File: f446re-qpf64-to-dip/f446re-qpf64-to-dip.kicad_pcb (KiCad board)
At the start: 2 copper layers, 34.5 x 83 mm, 3 parts, among them J1 Conn_01x32_Pin, J2 Conn_01x32_Pin, U1 STM32F446RETx

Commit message: change: GNDベタをやめた
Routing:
- added copper zone on F.Cu, net (none)
- removed copper zone on F.Cu, net GND
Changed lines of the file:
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@@
 		(tags "Through hole socket strip THT 1x32 2.54mm single row")
 		(property "Reference" "J2"
-			(at 0 -2.77 360)
+			(at 0 -2.77 0)
 			(layer "F.SilkS")
 			(hide yes)
@@
 		)
 		(property "Value" "Conn_01x32_Pin"
-			(at 0 81.51 360)
+			(at 0 81.51 0)
 			(layer "F.Fab")
 			(effects
@@
 	)
 	(zone
-		(net 60)
-		(net_name "GND")
+		(net 0)
+		(net_name "")
 		(layer "F.Cu")
 		(hatch edge 0.5)

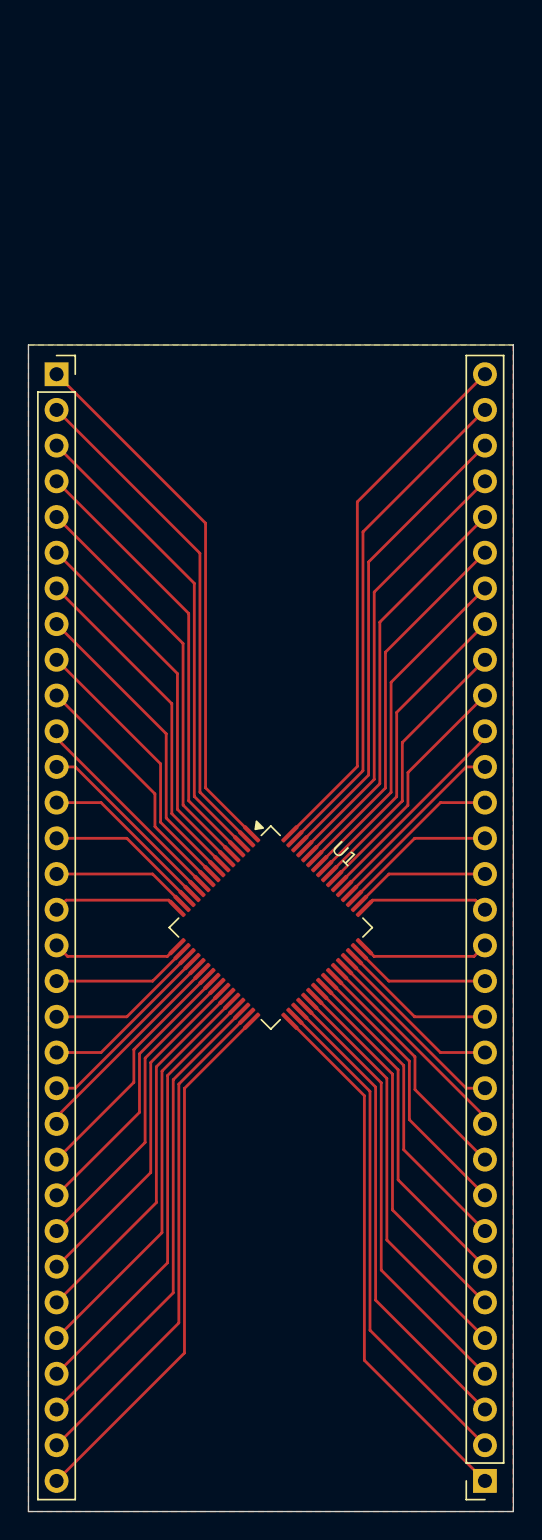
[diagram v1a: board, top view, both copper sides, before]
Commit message: change: 基盤サイズ変更
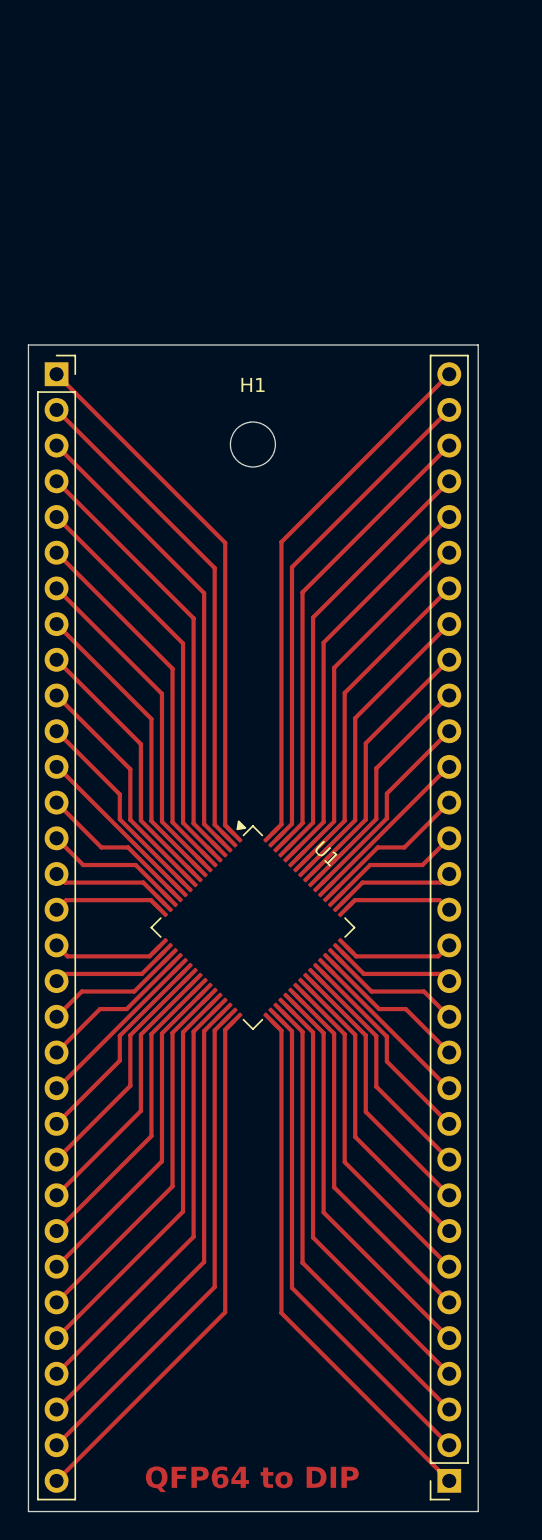
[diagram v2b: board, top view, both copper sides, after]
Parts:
- added H1: MountingHole, MountingHole:MountingHole_3.2mm_M3, F.Cu at (107.0, 88.6)
- moved J2 2.54 mm to (120.9, 162.3)
- moved U1 1.27 mm to (107.0, 123.0)
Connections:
- net GND renamed Net-(J1-Pin_18)
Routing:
- net Net-(J1-Pin_18): track 91.8 -> 88.2 mm
- net Net-(J2-Pin_21): track 13.6 -> 12.3 mm
- net Net-(J2-Pin_18): track 9.80 -> 8.53 mm
- net Net-(J2-Pin_12): track 13.6 -> 12.3 mm
- net Net-(J1-Pin_21): track 13.6 -> 12.3 mm
- net Net-(J1-Pin_12): track 13.6 -> 12.3 mm
- net Net-(J2-Pin_19): track 11.1 -> 9.79 mm
- net Net-(J2-Pin_14): track 11.1 -> 9.79 mm
- net Net-(J2-Pin_16): track 9.18 -> 7.91 mm
- net Net-(J2-Pin_13): track 12.3 -> 11.0 mm
- net Net-(J1-Pin_17): track 9.18 -> 7.91 mm
- net Net-(J1-Pin_14): track 11.1 -> 9.79 mm
- net Net-(J2-Pin_20): track 12.3 -> 11.0 mm
- net Net-(J1-Pin_13): track 12.3 -> 11.0 mm
- net Net-(J1-Pin_20): track 12.3 -> 11.0 mm
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- removed copper zone on F.Cu, net (none)
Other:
- board size 34.5 x 83 mm -> 32 x 83 mm
- board text added: "QFP64 to DIP"

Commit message: change: 配線変更
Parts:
- moved J2 21.2 mm to (117.0, 141.5)
- moved U1 20.9 mm to (105.6, 102.1)
- moved H1 20.9 mm to (105.6, 67.8)
- moved J1 20.9 mm to (94.2, 62.8)
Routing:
- net Net-(J1-Pin_18): track 88.2 -> 81.1 mm
- net Net-(J1-Pin_15): track 8.53 -> 5.99 mm
- net Net-(J1-Pin_14): track 9.79 -> 7.25 mm
- net Net-(J1-Pin_19): track 9.79 -> 7.25 mm
- net Net-(J2-Pin_19): track 9.79 -> 7.25 mm
- net Net-(J2-Pin_14): track 9.79 -> 7.25 mm
- net Net-(J2-Pin_18): track 8.53 -> 5.99 mm
- net Net-(J1-Pin_16): track 7.83 -> 5.44 mm
- net Net-(J2-Pin_17): track 7.83 -> 5.44 mm
- net Net-(J1-Pin_17): track 7.91 -> 5.64 mm
- net Net-(J2-Pin_16): track 7.91 -> 5.64 mm
- net Net-(J1-Pin_13): track 11.0 -> 8.88 mm
- net Net-(J1-Pin_20): track 11.0 -> 8.88 mm
- net Net-(J2-Pin_20): track 11.0 -> 8.88 mm
- net Net-(J2-Pin_13): track 11.0 -> 8.88 mm
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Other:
- board size 32 x 83 mm -> 26.7 x 82.6 mm
- board text removed: "QFP64 to DIP"

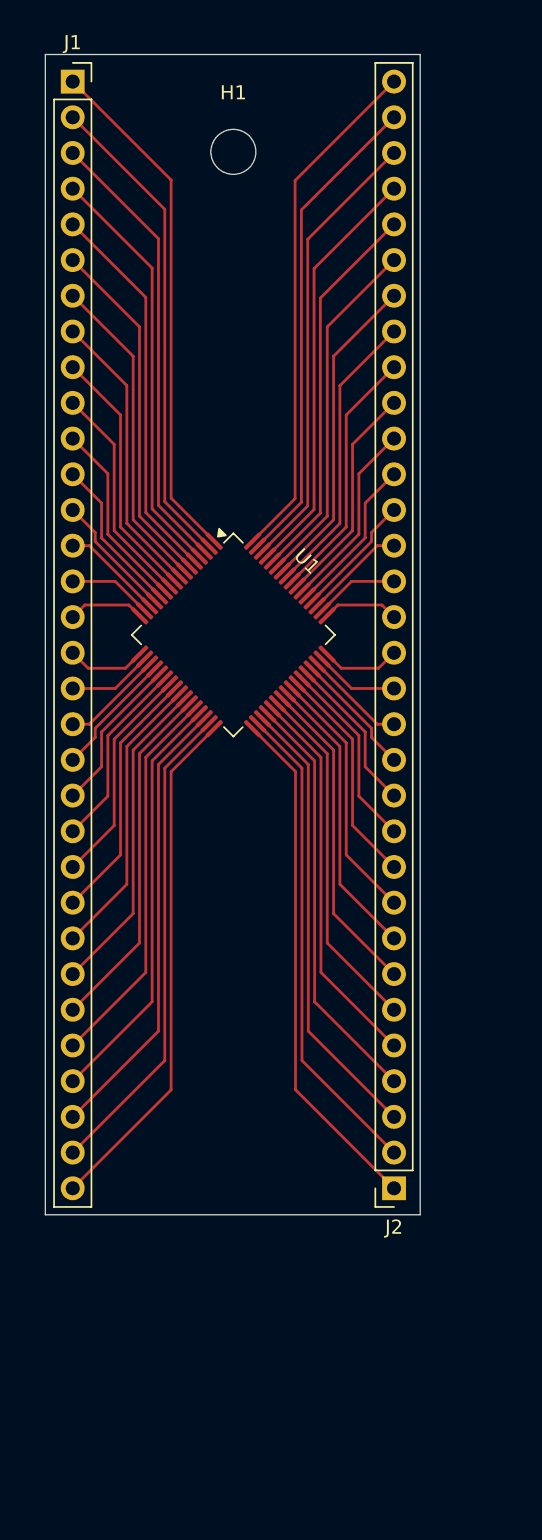
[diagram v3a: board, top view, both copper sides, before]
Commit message: change: 配線変更 & 文字追加
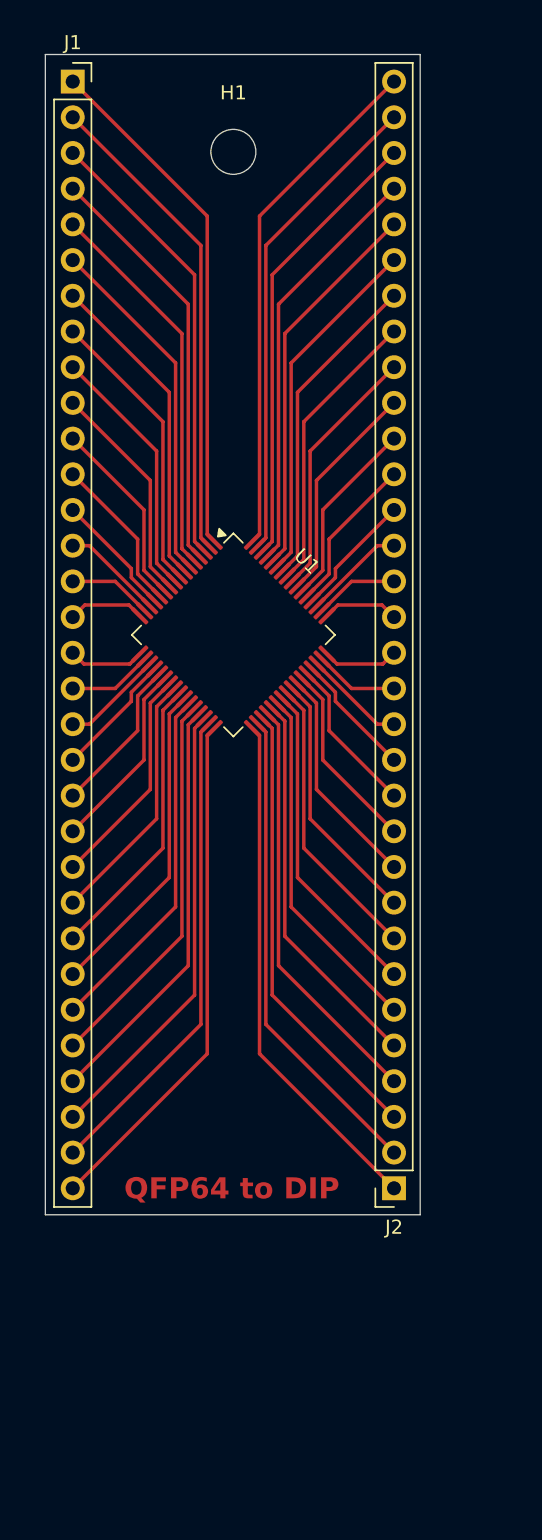
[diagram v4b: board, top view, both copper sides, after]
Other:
- board text added: "QFP64 to DIP"

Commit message: hoge
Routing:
- net Net-(J2-Pin_25): track 20.5 -> 21.6 mm
